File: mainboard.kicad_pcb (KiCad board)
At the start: 4 copper layers, 80 x 69.3 mm, 89 parts

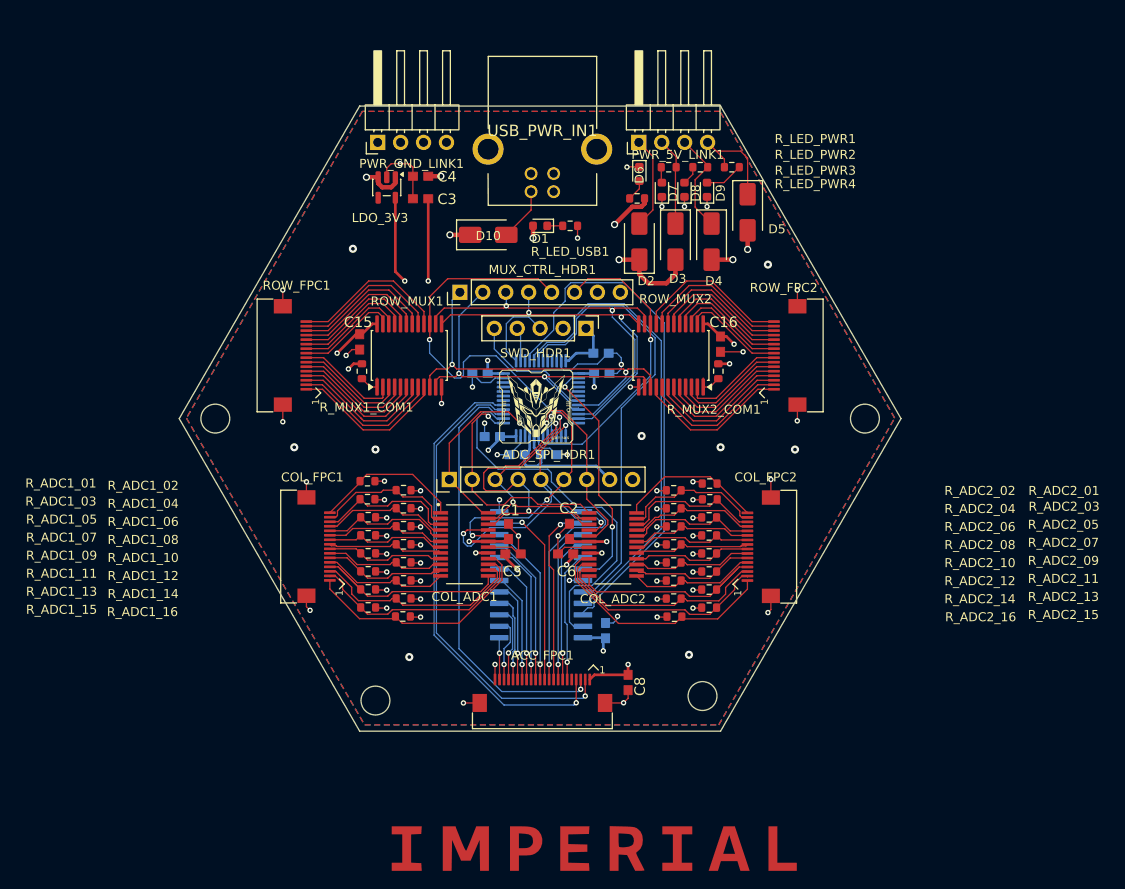
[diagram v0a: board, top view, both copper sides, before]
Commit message: Add hardware README and schematic documentation
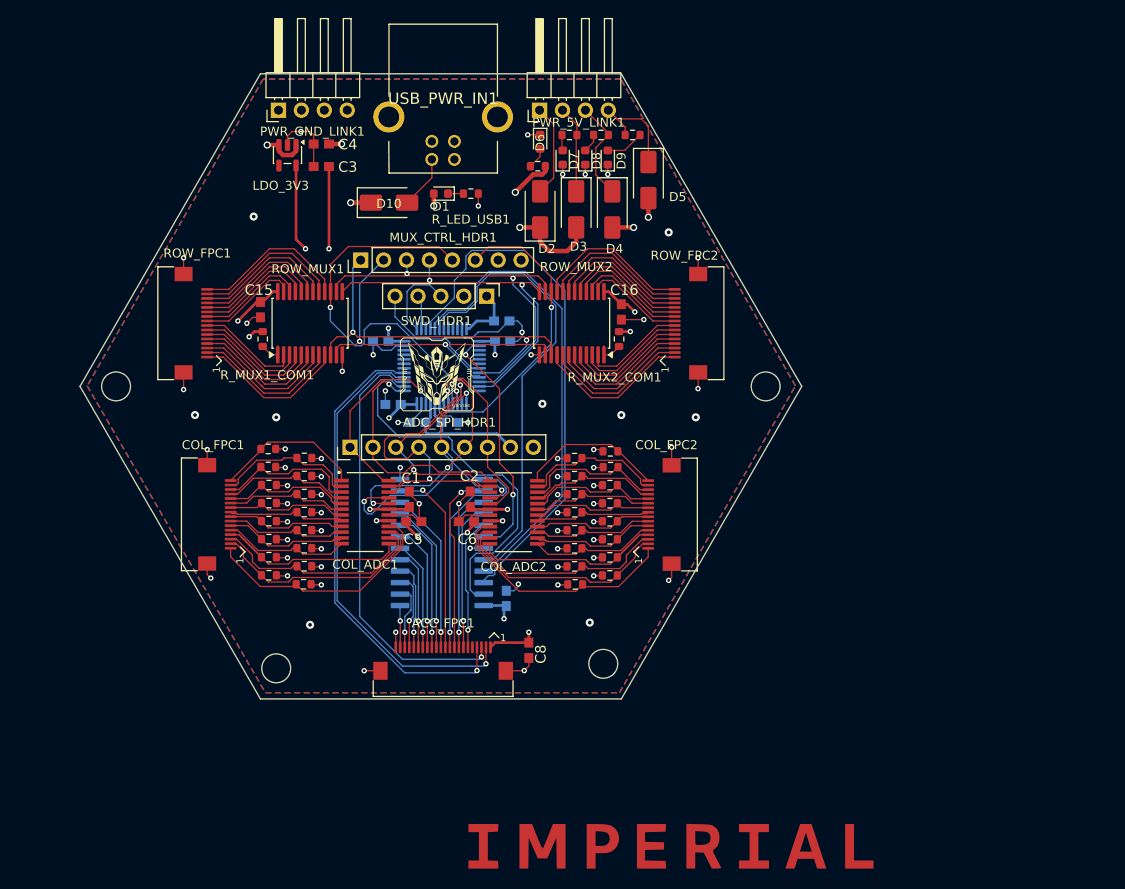
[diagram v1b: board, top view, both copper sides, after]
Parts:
- moved C10 11.6 mm to (106.5, 53.5)
- moved C15 11.6 mm to (79.8, 52.2)
- moved C16 11.6 mm to (119.8, 52.5)
- moved C3 11.6 mm to (86.5, 36.4)
- moved C4 11.6 mm to (86.5, 33.9)
- moved D1 11.6 mm to (99.8, 39.4)
- moved D10 11.6 mm to (94.0, 40.4)
- moved D2 11.6 mm to (110.8, 41.1)
- moved D3 11.6 mm to (114.8, 41.1)
- moved D4 11.6 mm to (118.8, 41.1)
- moved D5 11.6 mm to (122.8, 37.9)
- moved D6 11.6 mm to (110.8, 33.6)
- moved D7 11.6 mm to (113.2, 35.4)
- moved D8 11.6 mm to (115.8, 35.4)
- moved D9 11.6 mm to (118.2, 35.4)
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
